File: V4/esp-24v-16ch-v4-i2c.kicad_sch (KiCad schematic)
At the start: 25 parts, among them J8 NTC, U6 MCP23017_SS, U7 ADS1115IDGS, U8 MCP23017_SS, U9 SHT31-DIS

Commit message: Version 4.1
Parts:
- C26, U9: now fitted
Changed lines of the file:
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@@
 		(in_bom yes)
 		(on_board yes)
-		(dnp yes)
+		(dnp no)
 		(property "Reference" "C26"
 			(at 241.3 73.66 0)
@@
 		(in_bom yes)
 		(on_board yes)
-		(dnp yes)
+		(dnp no)
 		(fields_autoplaced yes)
 		(property "Reference" "U9"

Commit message: Revising schematics
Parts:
- removed C26: 100nF/50V, Tales:C_0402_1005Metric, symbol Device:C_Small
- removed U9: SHT31-DIS, Tales:Sensirion_DFN-8-1EP_2.5x2.5mm_P0.5mm_EP1.1x1.7mm, symbol Tales:SHT31-DIS
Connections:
- net +3.3V renamed +3V3
- no-connect marks 5 -> 3
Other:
- note removed: "TEMP/HUMID ADDRESS 0x44"

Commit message: Revising the schematics
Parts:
- R122: value 10k/62,5mW -> 10k
- R123: renamed from R128; value 680R/62,5mW -> 680R
- R124: renamed from R129; value 680R/62,5mW -> 680R
- R125: renamed from R124; value 10k/62,5mW -> 10k
- R126: renamed from R125; value 10k/62,5mW -> 10k
- R127: renamed from R123; value 10k/62,5mW -> 10k
- R128: renamed from R130; value 680R/62,5mW -> 680R
- R129: renamed from R131; value 680R/62,5mW -> 680R
- R24, R25: value 1k/62,5mW -> 1k
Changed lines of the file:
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@@
 		(dnp no)
 		(fields_autoplaced yes)
-		(property "Reference" "R128"
+		(property "Reference" "R123"
 			(at 146.05 149.86 90)
 			(effects
@@
 			)
 		)
-		(property "Value" "680R/62,5mW"
+		(property "Value" "680R"
 			(at 146.05 152.4 90)
 			(effects
@@
 			(project "esp-24v-16ch-v4"
 				(path "/2bc5a21a-1d79-419d-a592-6852cc07b00a/8d06b51d-d00b-4f80-9ffb-ab0131290cf2"
-					(reference "R128")
+					(reference "R123")
 					(unit 1)
 				)
@@
 		(dnp no)
 		(fields_autoplaced yes)
-		(property "Reference" "R123"
+		(property "Reference" "R127"
 			(at 97.79 191.7699 0)
 			(effects
@@
 			)
 		)
-		(property "Value" "10k/62,5mW"
+		(property "Value" "10k"
 			(at 97.79 194.3099 0)
 			(effects
@@
 			(project "esp-24v-16ch-v4"
 				(path "/2bc5a21a-1d79-419d-a592-6852cc07b00a/8d06b51d-d00b-4f80-9ffb-ab0131290cf2"
-					(reference "R123")
+					(reference "R127")
 					(unit 1)
 				)
@@
 		(on_board yes)
 		(dnp no)
-		(property "Reference" "R129"
+		(property "Reference" "R124"
 			(at 182.88 149.86 90)
 			(effects
@@
 			)
 		)
-		(property "Value" "680R/62,5mW"
+		(property "Value" "680R"
 			(at 182.88 152.4 90)
 			(effects
@@
 			(project "esp-24v-16ch-v4"
 				(path "/2bc5a21a-1d79-419d-a592-6852cc07b00a/8d06b51d-d00b-4f80-9ffb-ab0131290cf2"
-					(reference "R129")
+					(reference "R124")
 					(unit 1)
 				)
@@
 			)
 		)
-		(property "Value" "1k/62,5mW"
+		(property "Value" "1k"
 			(at 45.72 88.9 0)
 			(effects
@@
 		(dnp no)
 		(fields_autoplaced yes)
-		(property "Reference" "R130"
+		(property "Reference" "R128"
 			(at 146.05 194.31 90)
 			(effects
@@
 			)
 		)
-		(property "Value" "680R/62,5mW"
+		(property "Value" "680R"
 			(at 146.05 196.85 90)
 			(effects
@@
 			(project "esp-24v-16ch-v4"
 				(path "/2bc5a21a-1d79-419d-a592-6852cc07b00a/8d06b51d-d00b-4f80-9ffb-ab0131290cf2"
-					(reference "R130")
+					(reference "R128")
 					(unit 1)
 				)
@@
 		(dnp no)
 		(fields_autoplaced yes)
-		(property "Reference" "R125"
+		(property "Reference" "R126"
 			(at 116.84 181.6099 0)
 			(effects
@@
 			)
 		)
-		(property "Value" "10k/62,5mW"
+		(property "Value" "10k"
 			(at 116.84 184.1499 0)
 			(effects
@@
 			(project "esp-24v-16ch-v4"
 				(path "/2bc5a21a-1d79-419d-a592-6852cc07b00a/8d06b51d-d00b-4f80-9ffb-ab0131290cf2"
-					(reference "R125")
+					(reference "R126")
 					(unit 1)
 				)
@@
 			)
 		)
-		(property "Value" "10k/62,5mW"
+		(property "Value" "10k"
 			(at 92.71 151.1299 0)
 			(effects
@@
 			)
 		)
-		(property "Value" "1k/62,5mW"
+		(property "Value" "1k"
 			(at 146.05 88.9 0)
 			(effects
@@
 		(on_board yes)
 		(dnp no)
-		(property "Reference" "R131"
+		(property "Reference" "R129"
 			(at 182.88 194.31 90)
 			(effects
@@
 			)
 		)
-		(property "Value" "680R/62,5mW"
+		(property "Value" "680R"
 			(at 182.88 196.85 90)
 			(effects
@@
 			(project "esp-24v-16ch-v4"
 				(path "/2bc5a21a-1d79-419d-a592-6852cc07b00a/8d06b51d-d00b-4f80-9ffb-ab0131290cf2"
-					(reference "R131")
+					(reference "R129")
 					(unit 1)
 				)
@@
 		(dnp no)
 		(fields_autoplaced yes)
-		(property "Reference" "R124"
+		(property "Reference" "R125"
 			(at 116.84 168.9099 0)
 			(effects
@@
 			)
 		)
-		(property "Value" "10k/62,5mW"
+		(property "Value" "10k"
 			(at 116.84 171.4499 0)
 			(effects
@@
 			(project "esp-24v-16ch-v4"
 				(path "/2bc5a21a-1d79-419d-a592-6852cc07b00a/8d06b51d-d00b-4f80-9ffb-ab0131290cf2"
-					(reference "R124")
+					(reference "R125")
 					(unit 1)
 				)

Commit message: Rerouting
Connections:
- net I2C_SCL renamed I2CSCL
- net I2C_SDA renamed I2CSDA
- net MCP1-INTA renamed MCPININTA
- net MCP1-INTB renamed MCPININTB
- net VREF renamed AINVREF
- net /MCP_IN_RST renamed MCPINNRST
- net /MCP_OUT_RST renamed MCPOUTNRST
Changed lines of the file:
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@@
 		)
 	)
-	(label "{slash}MCP_IN_RST"
-		(at 52.07 86.36 0)
+	(label "MCPINNRST"
+		(at 53.34 86.36 0)
 		(effects
 			(font
@@
 		)
 	)
-	(label "{slash}MCP_OUT_RST"
-		(at 152.4 86.36 0)
+	(label "MCPOUTNRST"
+		(at 153.67 86.36 0)
 		(effects
 			(font
@@
 		)
 	)
-	(label "VREF"
-		(at 163.83 177.8 0)
+	(label "AINVREF"
+		(at 158.75 177.8 0)
 		(effects
 			(font
@@
 		)
 	)
-	(hierarchical_label "I2C_SDA"
+	(hierarchical_label "I2CSDA"
 		(shape bidirectional)
 		(at 370.84 29.21 0)
@@
 		)
 	)
-	(hierarchical_label "I2C_SCL"
+	(hierarchical_label "I2CSCL"
 		(shape input)
 		(at 370.84 31.75 0)
@@
 		)
 	)
-	(hierarchical_label "MCP1-INTA"
+	(hierarchical_label "MCPININTA"
 		(shape output)
 		(at 370.84 24.13 0)
@@
 		)
 	)
-	(hierarchical_label "MCP1-INTB"
+	(hierarchical_label "MCPININTB"
 		(shape output)
 		(at 370.84 26.67 0)

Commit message: Rerouting
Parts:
- added C26, C67: 100nF/50V, Tales:C_0402_1005Metric, symbol Device:C_Small
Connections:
- net +3V3: now also C26.1, C67.1
- net GND: now also C26.2, C67.2

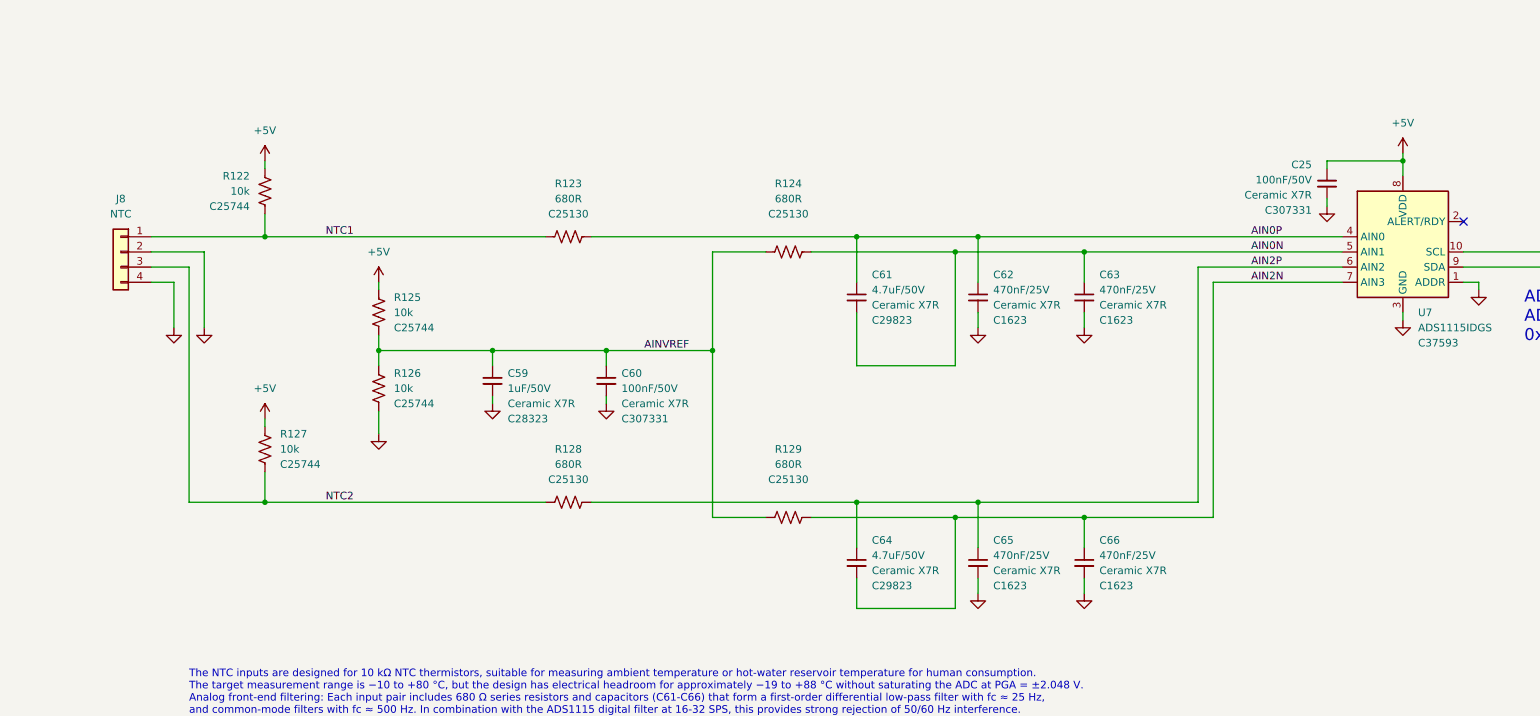
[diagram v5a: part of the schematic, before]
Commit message: Rerouting
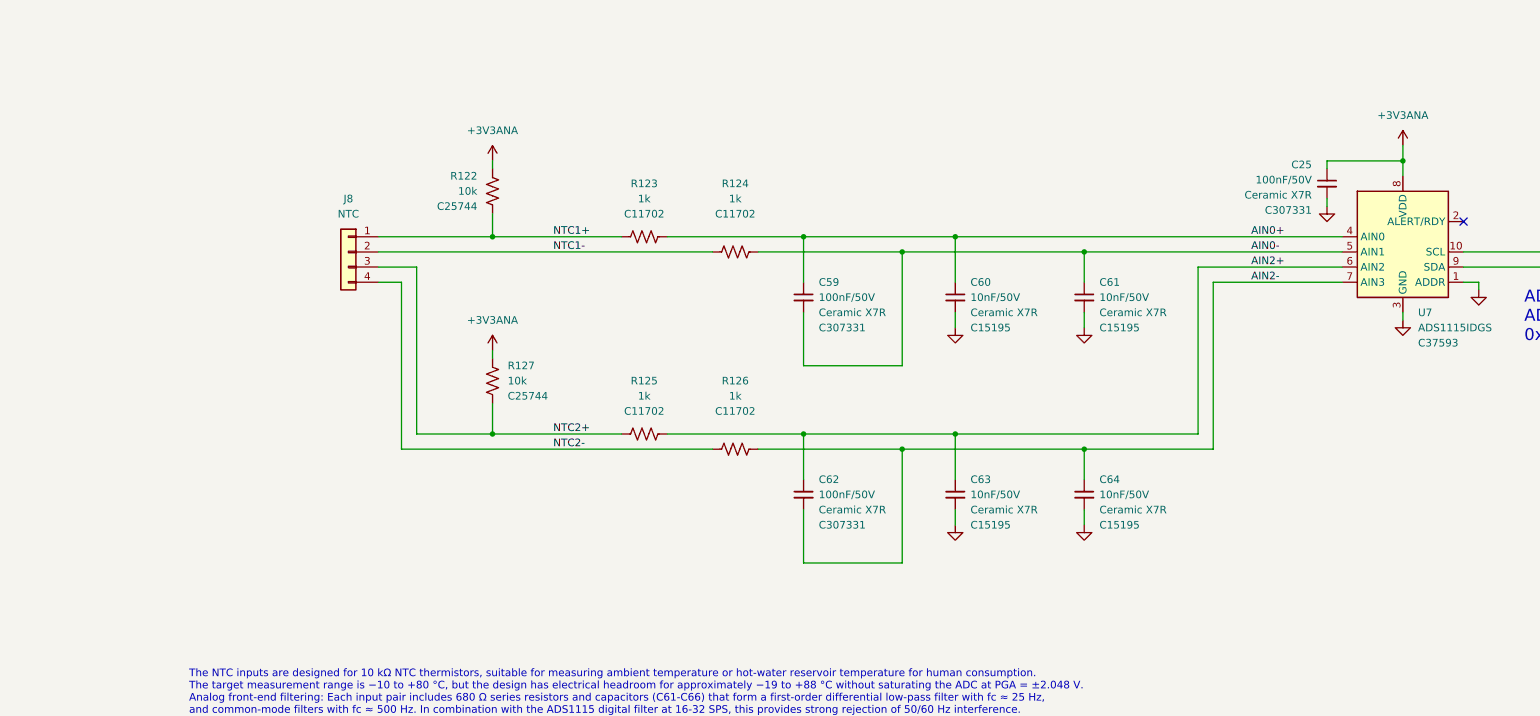
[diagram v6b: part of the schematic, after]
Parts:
- removed C65, C66: 470nF/25V, Tales:C_0603_1608Metric, symbol Device:C_Small
- removed R128, R129: 680R, Tales:R_0402_1005Metric, symbol Device:R_US
- C59: value 1uF/50V -> 100nF/50V; footprint Tales:C_0805_2012Metric -> Tales:C_0402_1005Metric; Case 0805/2012 -> 0402/1005; LCSC Part # C28323 -> C307331; Mfr PN CL21B105KBFNNNE -> CL05B104KB54PNC; Vendor PN C28323 -> C307331
- C60: value 100nF/50V -> 10nF/50V; LCSC Part # C307331 -> C15195; Mfr PN CL05B104KB54PNC -> CL05B103KB5NNNC; Vendor PN C307331 -> C15195
- C61, C64: value 4.7uF/50V -> 10nF/50V; footprint Tales:C_1206_3216Metric -> Tales:C_0402_1005Metric; Case 1206/3216 -> 0402/1005; LCSC Part # C29823 -> C15195; Mfr PN 1206B475K500NT -> CL05B103KB5NNNC; Package 1206/3216 -> 0402/1005; Vendor PN C29823 -> C15195
- C62: value 470nF/25V -> 100nF/50V; footprint Tales:C_0603_1608Metric -> Tales:C_0402_1005Metric; Case 0603/1608 -> 0402/1005; LCSC Part # C1623 -> C307331; Mfr PN CL10B474KA8NNNC -> CL05B104KB54PNC; Package 0603/1608 -> 0402/1005; Vendor PN C1623 -> C307331
- C63: value 470nF/25V -> 10nF/50V; footprint Tales:C_0603_1608Metric -> Tales:C_0402_1005Metric; Case 0603/1608 -> 0402/1005; LCSC Part # C1623 -> C15195; Mfr PN CL10B474KA8NNNC -> CL05B103KB5NNNC; Package 0603/1608 -> 0402/1005; Vendor PN C1623 -> C15195
- R123, R124: value 680R -> 1k; LCSC Part # C25130 -> C11702; Mfr PN 0402WGF6800TCE -> 0402WGF1001TCE; Package 0402/1005 -> (none); Vendor PN C25130 -> C11702
- R125, R126: value 10k -> 1k; LCSC Part # C25744 -> C11702; Mfr PN 0402WGF1002TCE -> 0402WGF1001TCE; Package 0402/1005 -> (none); Vendor PN C25744 -> C11702
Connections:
- net GND: now also C61.2, C64.2; no longer C59.2, C62.2, J8.2 (Pin_2), J8.4 (Pin_4), R126.1
- net +5V renamed +3V3ANA
- net +3V3ANA: no longer R125.2
- net AIN0N renamed AIN0-
- net AIN0-: now also C59.2, C61.1; no longer C61.2, C63.1
- net AIN0P renamed AIN0+
- net AIN0+: now also C59.1, C60.1; no longer C61.1, C62.1
- net AIN2N renamed AIN2-
- net AIN2-: now also C62.2, C64.1, R126.1; no longer C64.2
- net AIN2P renamed AIN2+
- net AIN2+: now also C62.1, C63.1, R125.1; no longer C64.1
- removed net AINVREF: C59.1, C60.1, R124.2, R125.1, R126.2
- net NTC1 renamed NTC1+
- net NTC2 renamed NTC2+
- net NTC2+: now also R125.2
- new net NTC1-: J8.2 (Pin_2), R124.2
- new net NTC2-: J8.4 (Pin_4), R126.2
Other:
- moved on the sheet: J8, R122, R127

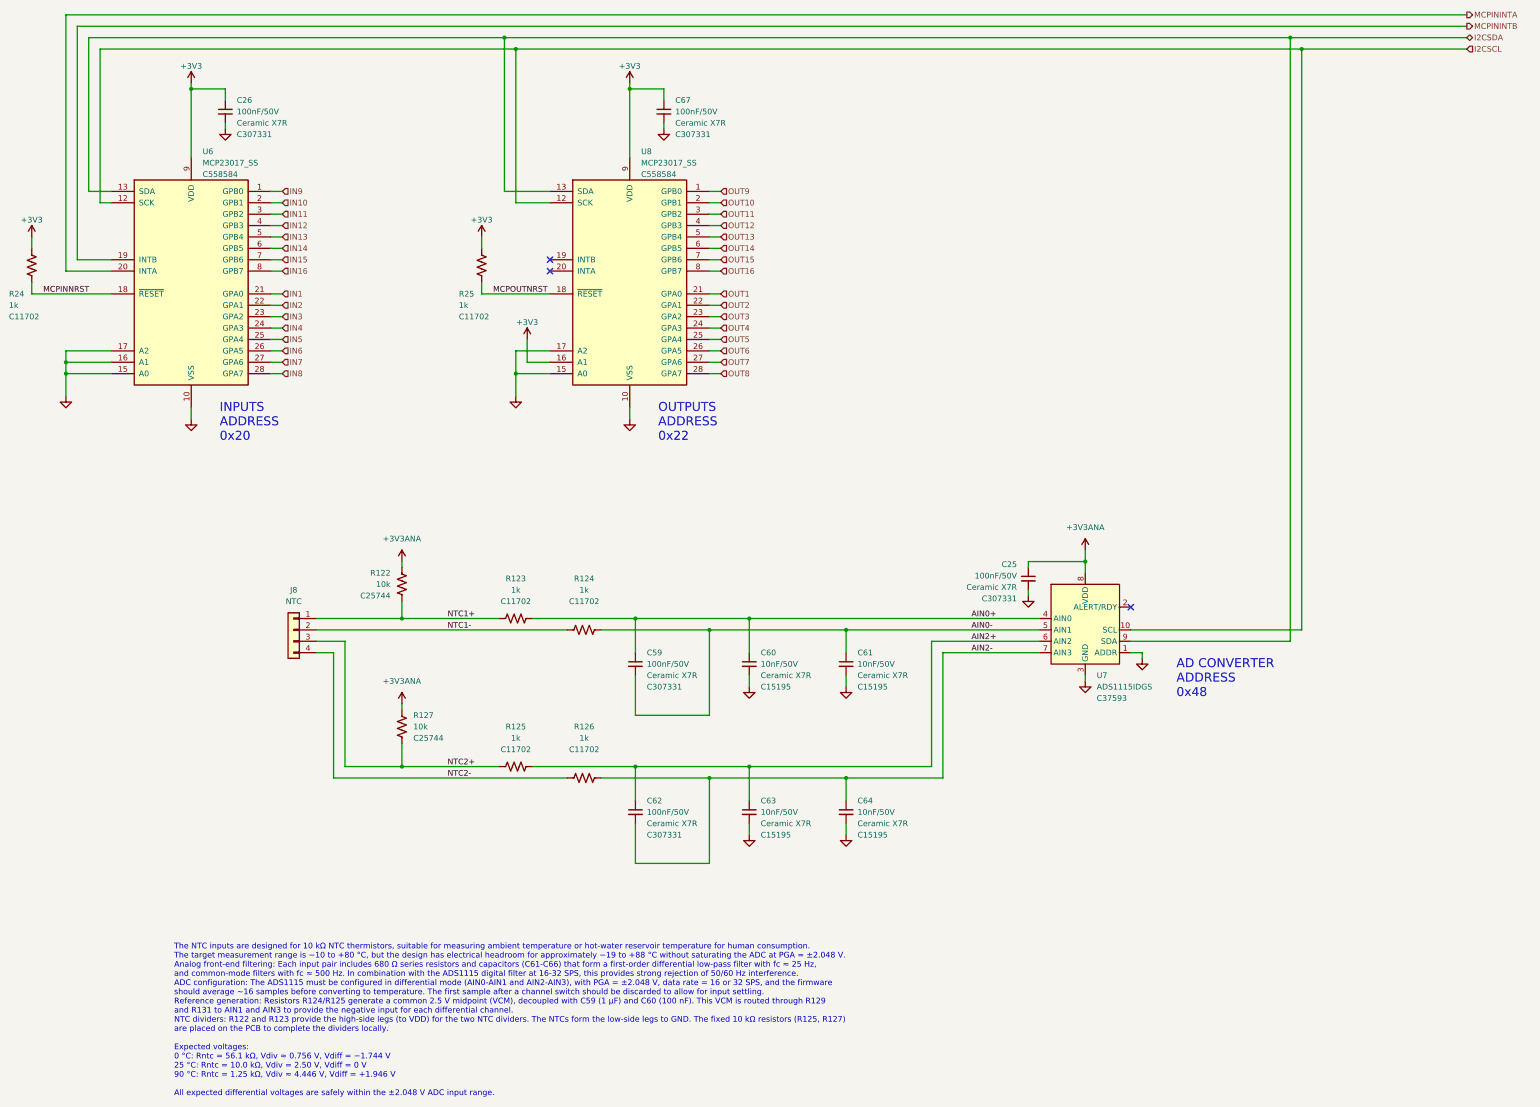
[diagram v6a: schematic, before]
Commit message: Rerouting
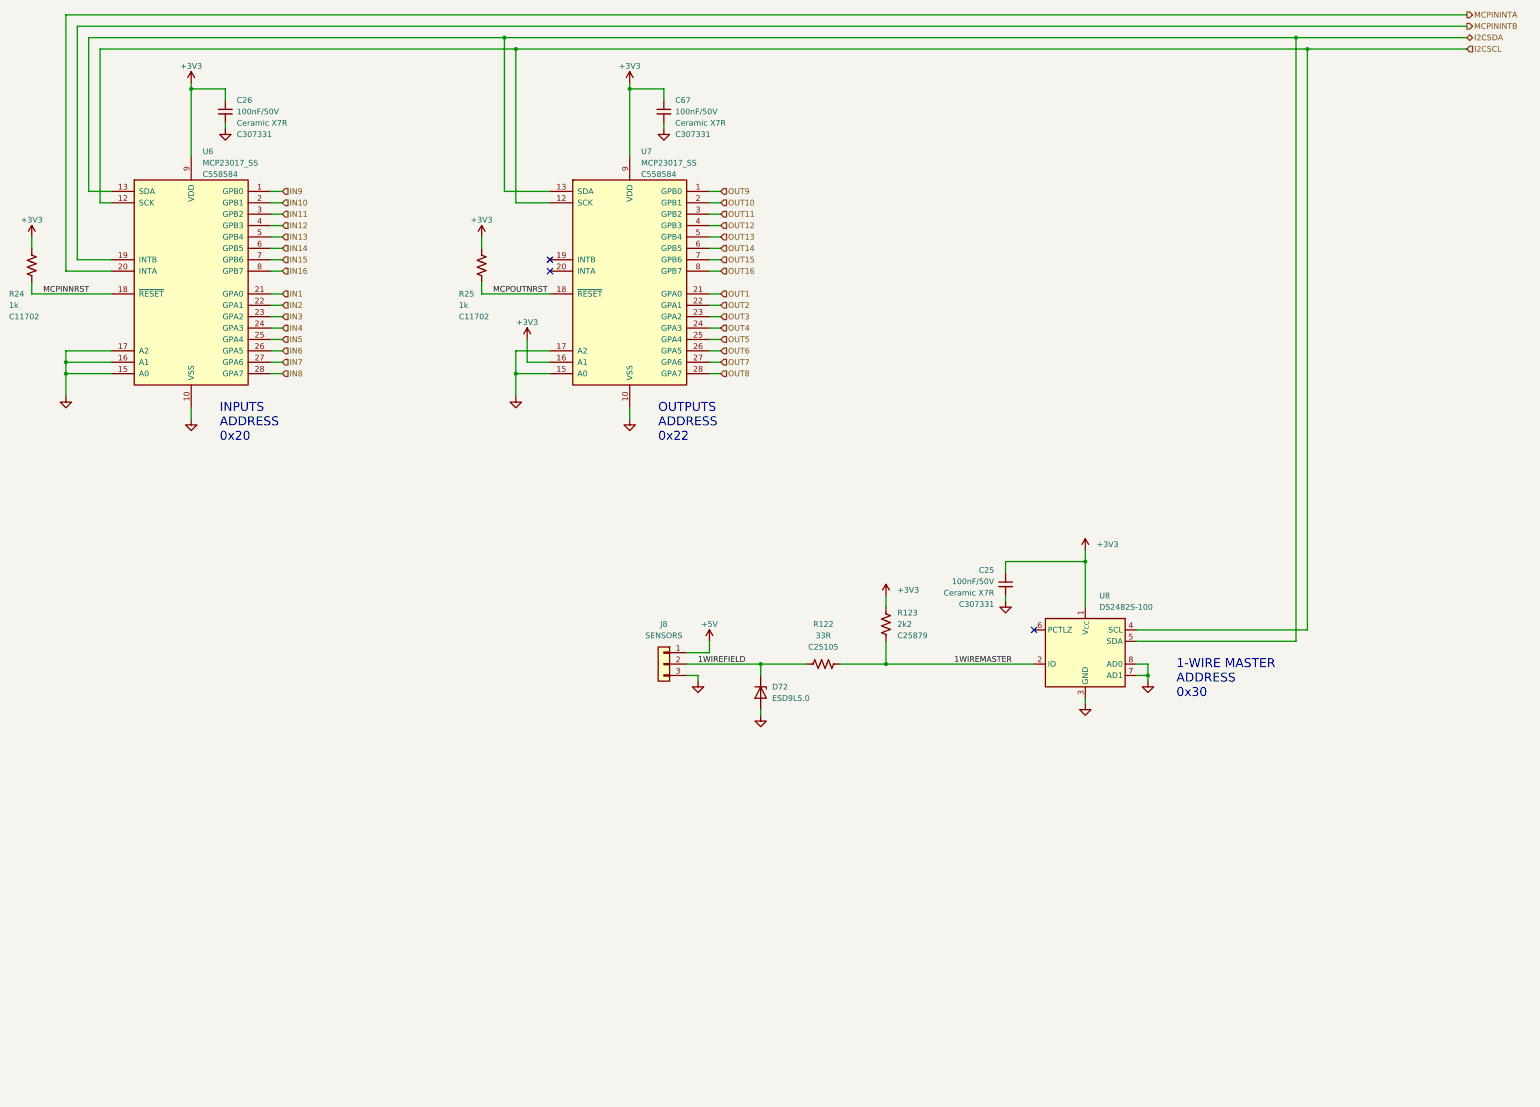
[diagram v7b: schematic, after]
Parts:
- removed C59, C62: 100nF/50V, Tales:C_0402_1005Metric, symbol Device:C_Small
- removed C60, C61, C63, C64: 10nF/50V, Tales:C_0402_1005Metric, symbol Device:C_Small
- removed R124, R125, R126: 1k, Tales:R_0402_1005Metric, symbol Device:R_US
- removed R127: 10k, Tales:R_0402_1005Metric, symbol Device:R_US
- removed U7: ADS1115IDGS, Package_SO:TSSOP-10_3x3mm_P0.5mm, symbol Analog_ADC:ADS1115IDGS
- added D72: ESD9L5.0, Diode_SMD:D_SOD-923, symbol Diode:ESD5Zxx
- added U8: DS2482S-100, Package_SO:SO-8_3.9x4.9mm_P1.27mm, symbol Tales:DS2482-100
- J8: value NTC -> SENSORS; footprint Tales:TerminalBlock_Dibo_DB141V-2.54-4P_1x04_P2.54mm_Vertical -> Tales:TerminalBlock_Dibo_DB141V-2.54-3P_1x03_P2.54mm_Vertical; symbol Connector_Generic:Conn_01x04 -> Connector_Generic:Conn_01x03; LCSC Part # C2898746 -> C2898745; Mfr PN DB141V-2.54-4P -> DB141V-2.54-3P-GN; Vendor PN C2898746 -> C2898745
- R122: value 10k -> 33R; LCSC Part # C25744 -> C25105; Mfr PN 0402WGF1002TCE -> 0402WGF330JTCE; Package 0402/1005 -> (none); Vendor PN C25744 -> C25105
- R123: value 1k -> 2k2; LCSC Part # C11702 -> C25879; Mfr PN 0402WGF1001TCE -> 0402WGF2201TCE; Vendor PN C11702 -> C25879
- renumbered U8 to U7
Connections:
- net AIN0+ is gone; now on net +3V3: R123.1
- net NTC2+ is gone; now on net GND: J8.3 (Pin_3)
- net +3V3: now also C25.1, U8.1 (V_{CC})
- net GND: now also D72.2 (A), U8.3 (GND), U8.7 (AD1), U8.8 (AD0)
- net I2CSCL: now also U8.4 (SCL)
- net I2CSDA: now also U8.5 (SDA)
- net +3V3ANA renamed 1WIREMASTER
- net 1WIREMASTER: now also R123.2, U8.2 (IO); no longer C25.1
- removed net NTC1+: J8.1 (Pin_1), R122.1, R123.2
- net NTC1- renamed 1WIREFIELD
- net 1WIREFIELD: now also R122.1, D72.1 (K)
- removed net NTC2-: J8.4 (Pin_4)
- new net +5V: J8.1 (Pin_1)
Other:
- note added: "1-WIRE MASTER ADDRESS 0x30"
- note removed: "AD CONVERTER ADDRESS 0x48"
- note removed: "The NTC inputs are designed for 10 kΩ NTC thermistors, suitable for measuring ambient temperature or hot-water reservoir temperature for human consumption. The target measurement range is −10 to +80 °C, but the design has electrical headroom for approximately −19 to +88 °C without saturating the ADC at PGA = ±2.048 V. Analog front-end filtering: Each input pair includes 680 Ω series resistors and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"
- moved on the sheet: C25
